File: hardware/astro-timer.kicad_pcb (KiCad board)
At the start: 2 copper layers, 65.8 x 41.4 mm, 36 parts, among them J1 AVR-ISP-6, J2 AudioJack3, Q1 Q_NPN_BEC, Q2 Q_NPN_BEC, SW1 SW_SPST, SW2 SW_Push, SW3 SW_Push, SW4 Rotary_Encoder_Switch, U1 ATmega328P-AU, Y1 Crystal

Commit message: ducklings
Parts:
- moved C4 4.61 mm to (122.6, 121.5)
- moved R12 3.35 mm to (130.2, 121.5)
- moved R13 2.03 mm to (140.6, 121.5), turned to 0 degrees
- moved C3 1.89 mm to (126.5, 121.5)
- moved R14 1.28 mm to (137.2, 121.5), turned to 0 degrees
- moved R11 0.84 mm to (133.7, 121.5)
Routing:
- net VCC: track 109.4 -> 113.4 mm
- net GND: track 32.3 -> 35.0 mm
- net Net-(R12-Pad1): track 10.0 -> 11.9 mm
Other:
- board text added: "astrophoto timer v4.1 by Jeremy Stanley"
- board text removed: "astrophoto timer v4.0 by Jeremy Stanley"

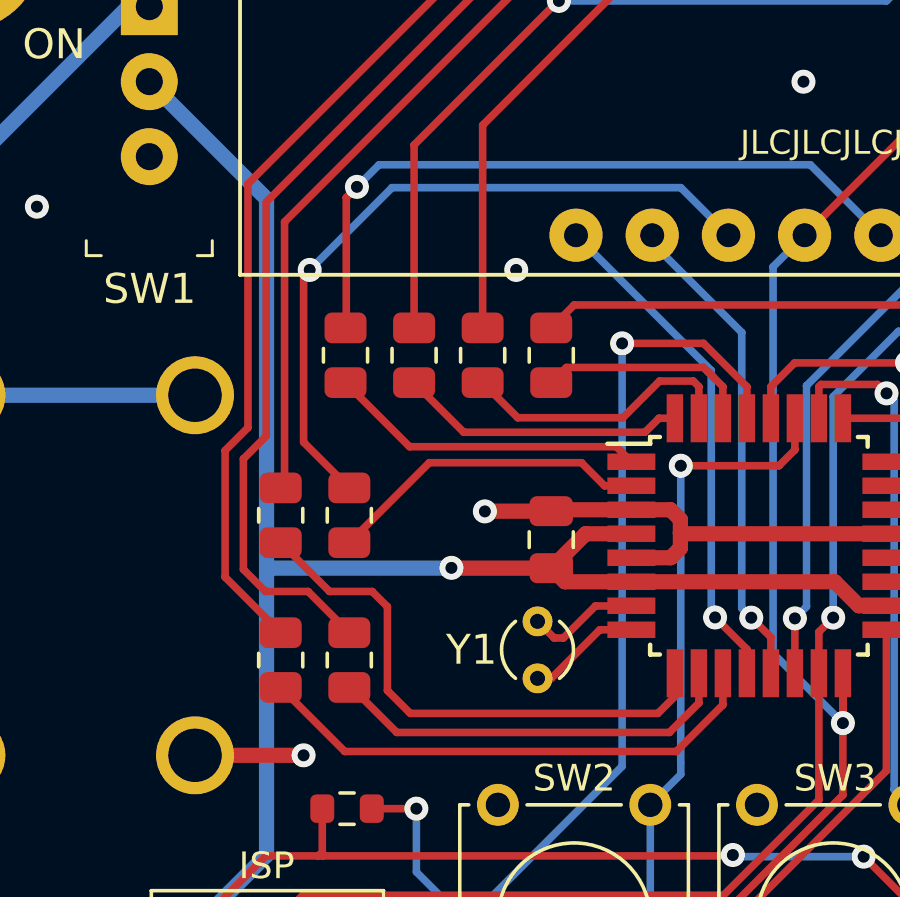
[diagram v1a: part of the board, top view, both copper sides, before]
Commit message: add a bit more clearance from R1 and R2 to the battery
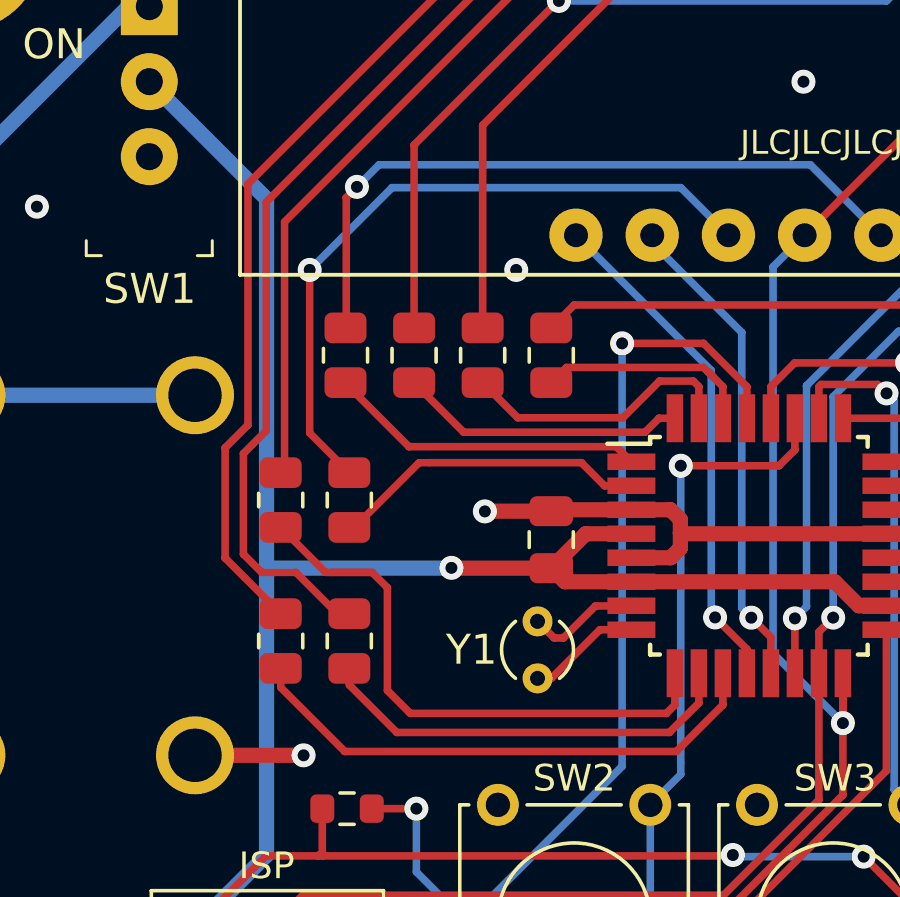
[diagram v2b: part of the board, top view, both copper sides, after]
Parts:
- moved R1 0.64 mm to (96.5, 113.2)
- moved R2 0.64 mm to (98.7, 113.2)
- moved R3 0.51 mm to (96.5, 108.5)
- moved R4 0.51 mm to (98.7, 108.5)
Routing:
- net /c: track 18.1 -> 18.9 mm
- net /a: track 17.3 -> 18.0 mm
- net Net-(LED1-Pad12): track 43.1 -> 42.4 mm
- net /b: track 13.7 -> 14.3 mm
- net Net-(LED1-Pad16): track 31.0 -> 30.5 mm
- net Net-(LED1-Pad13): track 41.6 -> 41.1 mm

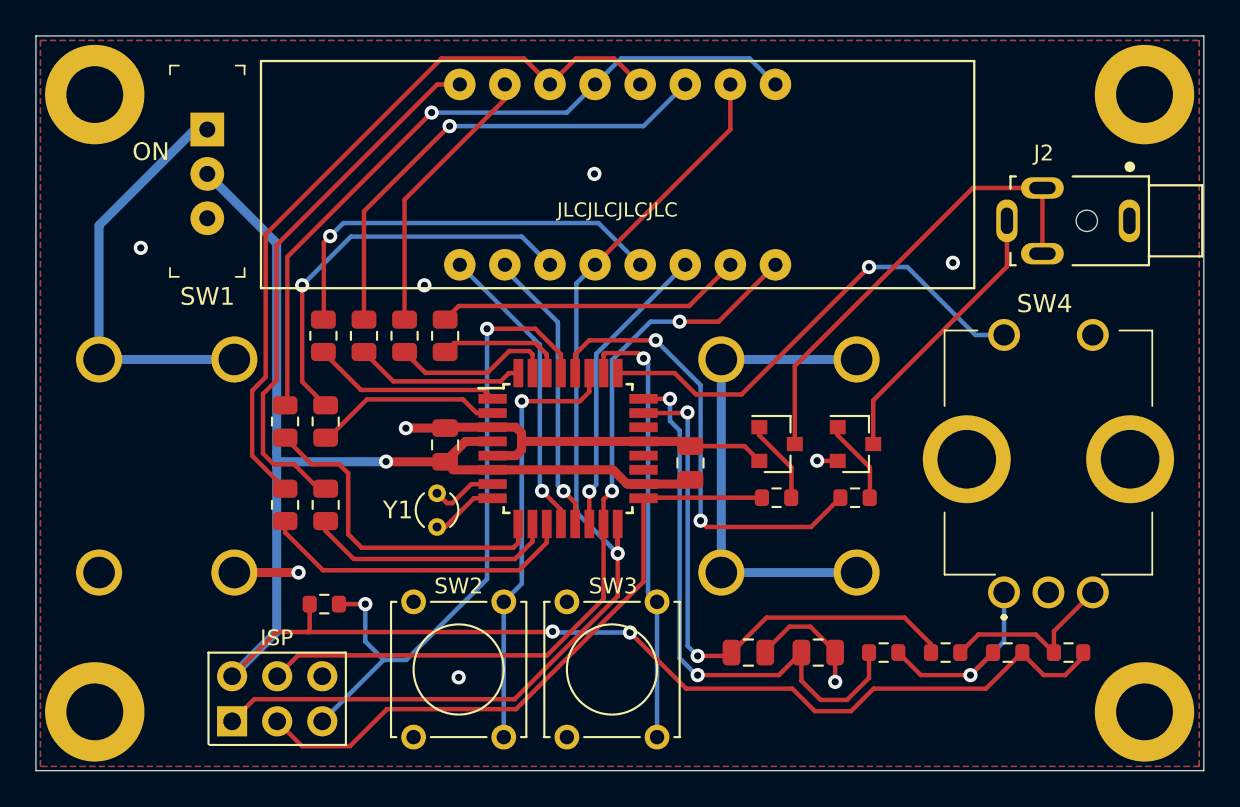
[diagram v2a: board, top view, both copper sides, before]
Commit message: a bit more clearance
and why did I like the duckling arrangement
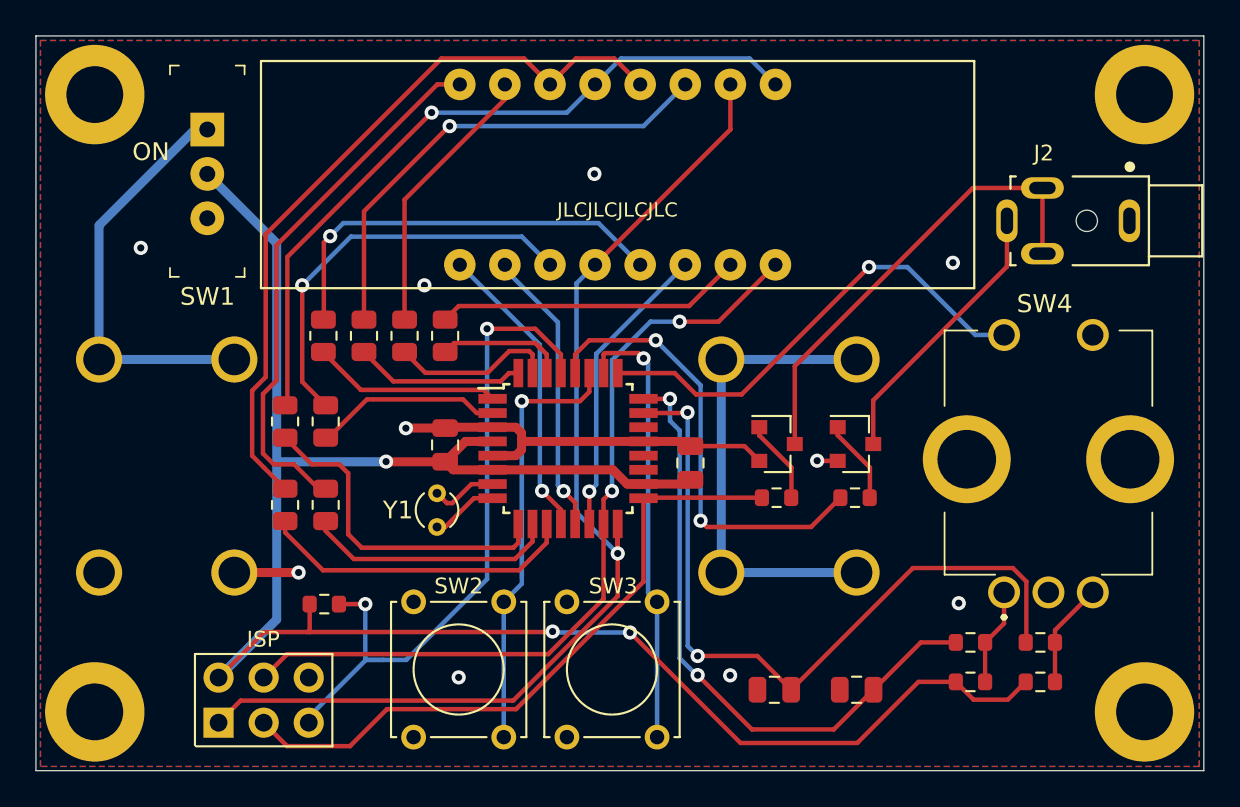
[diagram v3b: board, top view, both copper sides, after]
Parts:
- moved R11 5.36 mm to (139.0, 121.0)
- moved R12 4.92 mm to (135.1, 121.0)
- moved C3 3.01 mm to (128.7, 123.6), turned to 180 degrees
- moved R14 2.67 mm to (135.1, 123.2), turned to 180 degrees
- moved C4 2.55 mm to (124.0, 123.6), turned to 180 degrees
- moved R13 2.29 mm to (139.0, 123.2), turned to 180 degrees
- moved J1 0.77 mm to (92.7, 125.5)
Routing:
- net /enc_a: track 31.7 -> 42.4 mm
- net GND: track 35.0 -> 28.1 mm, vias 9 -> 10
- net Net-(R12-Pad1): track 11.9 -> 5.50 mm, vias 1 -> 0
- net Net-(R11-Pad1): track 11.7 -> 7.04 mm
- net /enc_b: track 31.9 -> 35.6 mm
- net VCC: track 113.4 -> 111.7 mm
- net /rst: track 37.6 -> 39.2 mm
- net /dige: track 61.3 -> 62.1 mm
- net /dig4: track 45.3 -> 46.1 mm
- net /cam-shutter: track 36.4 -> 37.2 mm

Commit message: tweaks
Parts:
- moved R1 5.31 mm to (91.6, 111.0)
- moved R2 5.26 mm to (94.0, 111.0)
- moved R3 2.49 mm to (96.3, 111.0)
- moved R4 2.49 mm to (98.6, 111.0)
- moved C3 0.53 mm to (128.7, 123.1)
- moved C4 0.53 mm to (124.0, 123.1)
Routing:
- net /b: track 14.3 -> 20.0 mm
- net /a: track 18.0 -> 23.3 mm
- net Net-(LED1-Pad16): track 30.5 -> 26.4 mm
- net Net-(LED1-Pad3): track 23.3 -> 26.1 mm
- net Net-(LED1-Pad13): track 41.1 -> 43.7 mm
- net /c: track 18.9 -> 16.5 mm
- net Net-(LED1-Pad12): track 42.4 -> 40.7 mm
- net /d: track 10.6 -> 12.2 mm

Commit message: tweaks
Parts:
- moved R1 0.15 mm to (91.8, 111.0)
- moved R2 0.10 mm to (94.1, 111.0)
- moved R3 0.05 mm to (96.4, 111.0)
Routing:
- net /d: track 12.2 -> 12.9 mm

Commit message: tweaks!
this is a perfectionist's black hole
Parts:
- moved C3 1.71 mm to (126.9, 123.1), turned to 90 degrees
- moved C4 0.51 mm to (123.5, 123.1), turned to 270 degrees
- moved Q1 0.20 mm to (124.1, 110.0)
- moved Q2 0.20 mm to (128.6, 110.0)
- moved R10 0.18 mm to (128.6, 113.0)
- moved R9 0.18 mm to (124.1, 113.0)
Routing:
- net GND: track 27.8 -> 24.1 mm, vias 10 -> 9
- net /enc_b: track 35.1 -> 37.0 mm
- net /enc_a: track 42.0 -> 41.2 mm

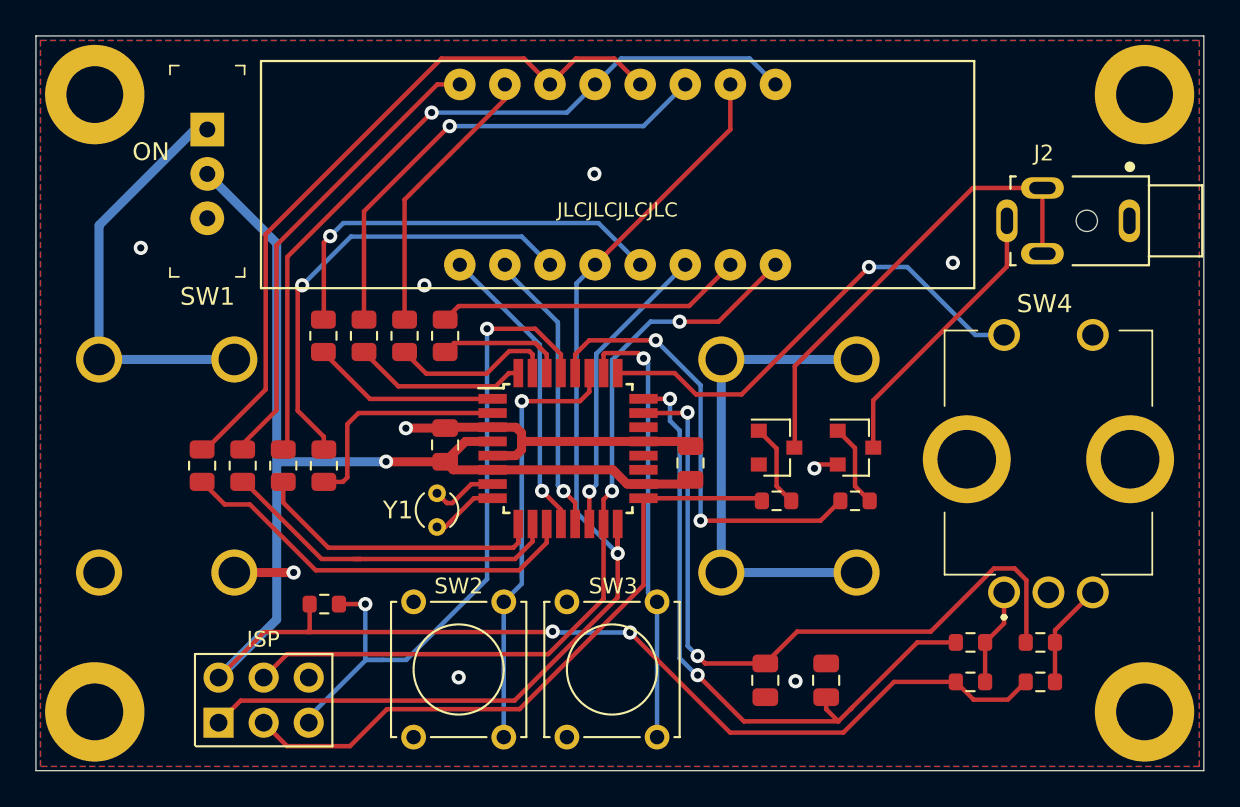
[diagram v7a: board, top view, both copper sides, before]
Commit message: label things
I thought I didn't need them on parts I was going to have
the PCB house mount, but it occurs to me that if they fail to
do so for whatever reason, it'd be nice to know what goes where
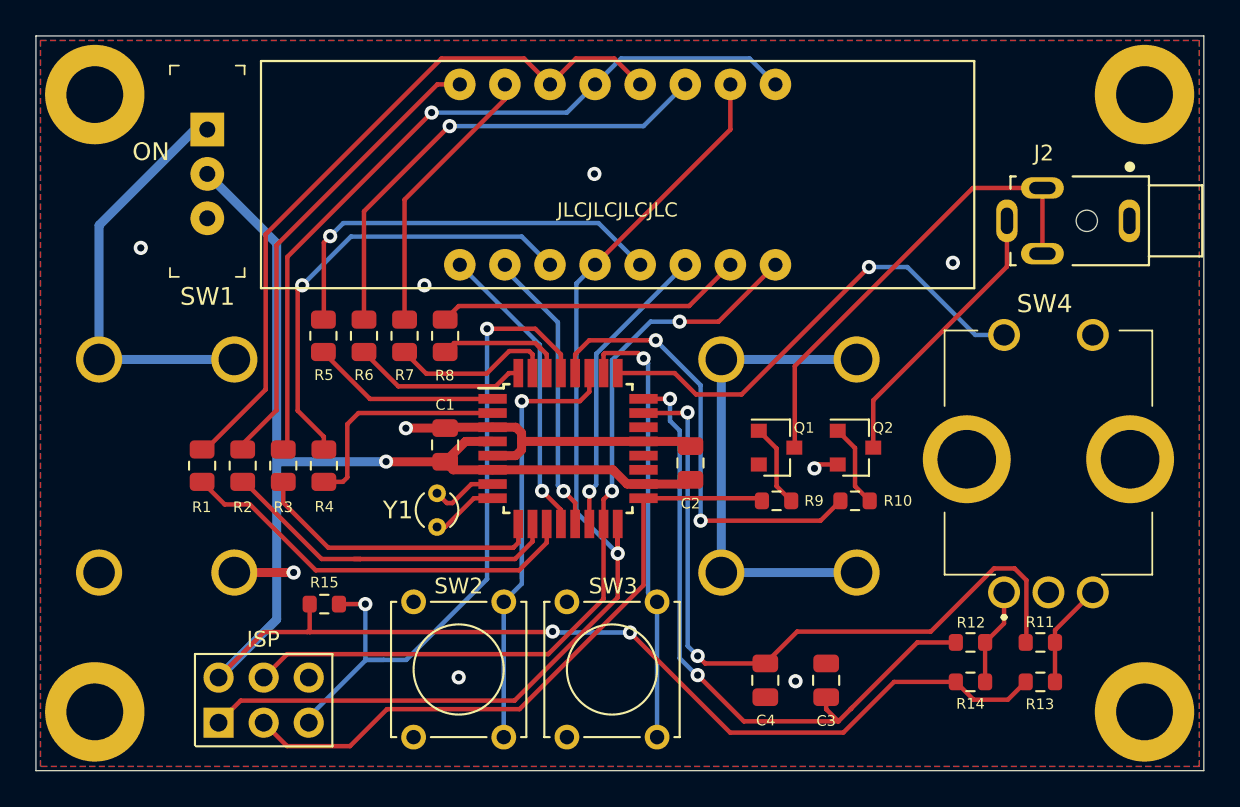
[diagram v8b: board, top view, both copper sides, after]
